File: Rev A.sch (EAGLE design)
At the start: 18 parts

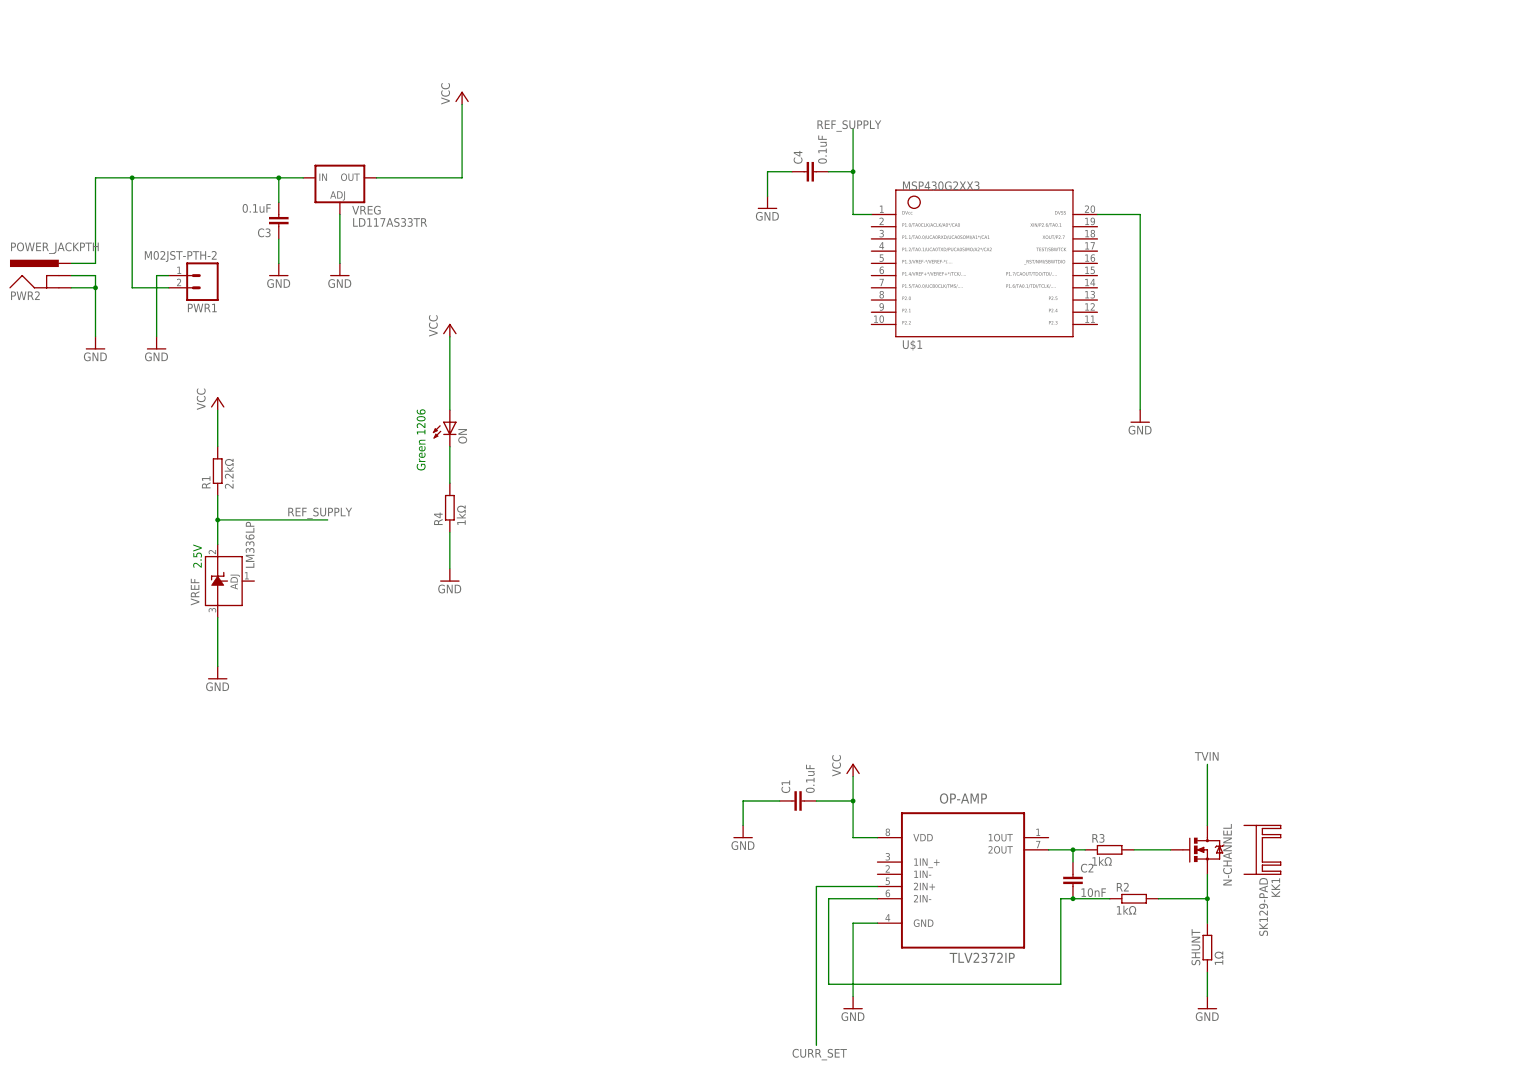
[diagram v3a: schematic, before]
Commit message: Added the PWM filtering circuit
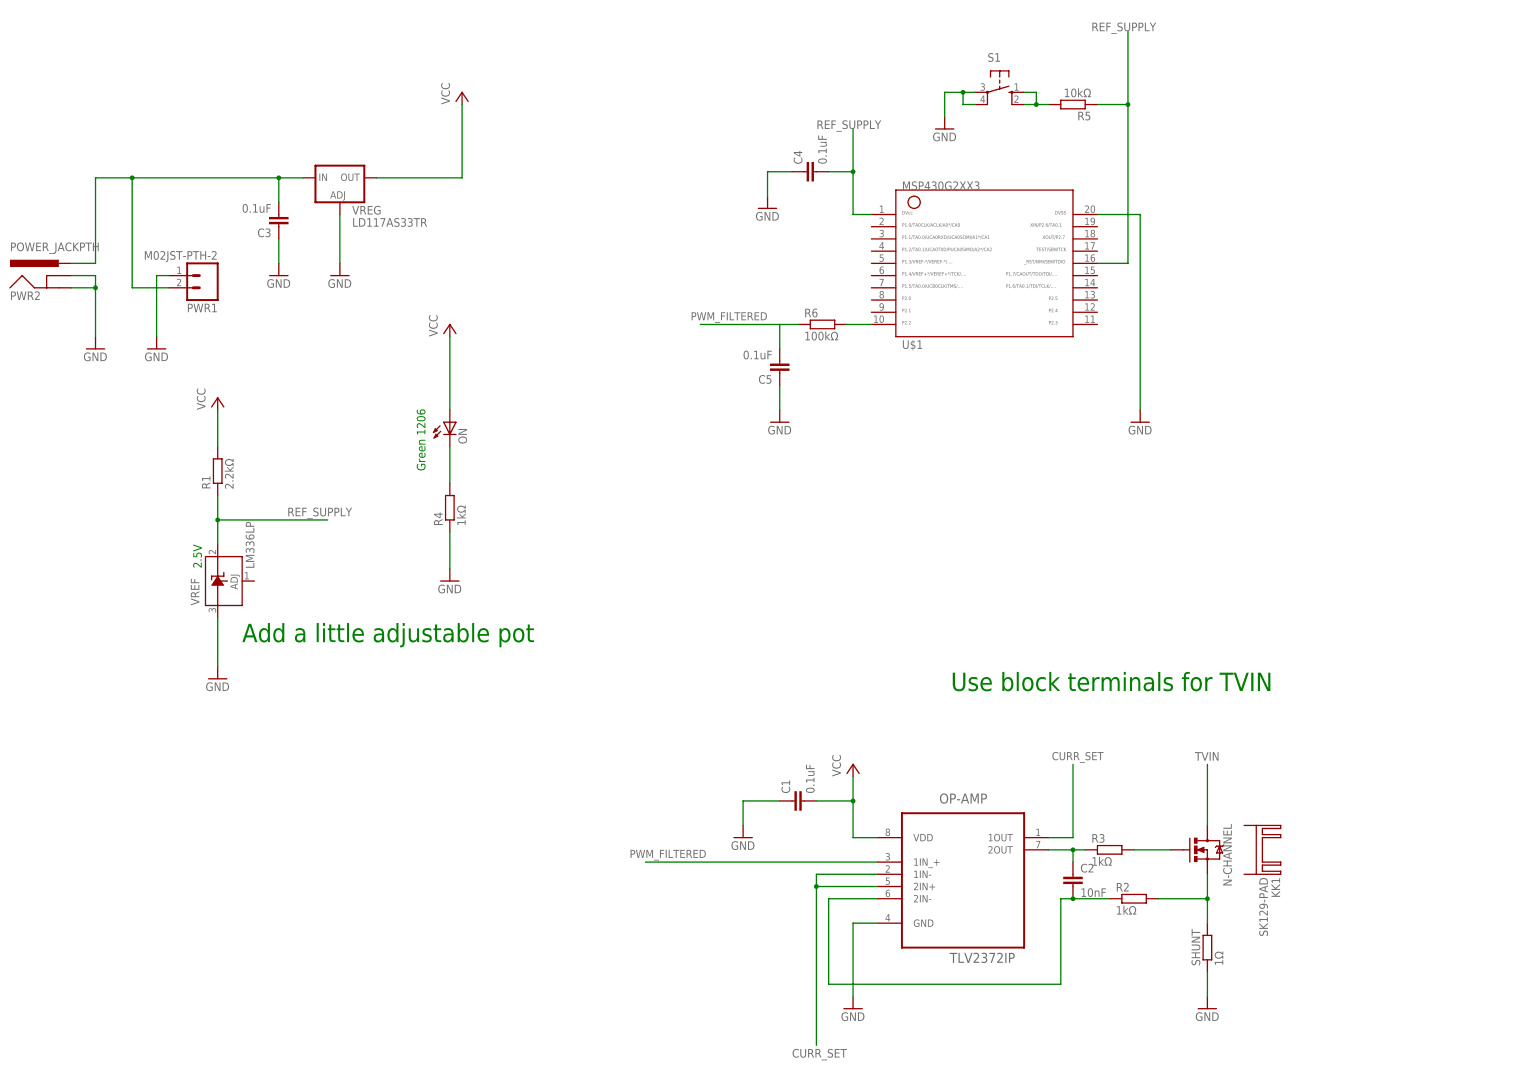
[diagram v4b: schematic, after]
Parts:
- added C5: 0.1uF, rcl:C-EUC0805
- added R5: 10kΩ, resistor:R-EU_R0805
- added R6: 100kΩ, rcl:R-EU_R0805
- added S1: (no value), switch-omron:10-XX
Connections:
- new net N$5: R5.2, S1.S, S1.S1
- new net N$8: R6.2, U$1.10
- new net PWM_FILTERED: C5.2, OP-AMP.1IN_+, R6.1
- net CURR_SET: now also OP-AMP.1IN-, OP-AMP.1OUT
- net GND: now also C5.1, S1.P, S1.P1
- net REF_SUPPLY: now also R5.1, U$1.16
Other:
- note added: "Add a little adjustable pot"
- note added: "Use block terminals for TVIN"
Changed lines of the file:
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@@
 <part name="GND11" library="supply1" deviceset="GND" device=""/>
 <part name="C4" library="rcl" deviceset="C-EU" device="C0805" value="0.1uF"/>
+<part name="S1" library="switch-omron" deviceset="10-XX" device=""/>
+<part name="R5" library="resistor" deviceset="R-EU_" device="R0805" value="10kΩ"/>
+<part name="GND12" library="supply1" deviceset="GND" device=""/>
+<part name="C5" library="rcl" deviceset="C-EU" device="C0805" value="0.1uF"/>
+<part name="R6" library="rcl" deviceset="R-EU_" device="R0805" value="100kΩ"/>
+<part name="GND13" library="supply1" deviceset="GND" device=""/>
 </parts>
 <sheets>
@@
 <text x="-7.62" y="96.52" size="1.778" layer="91" rot="R270">2.5V</text>
 <text x="40.64" y="111.76" size="1.778" layer="91" rot="R90">Green 1206</text>
+<text x="2.54" y="76.2" size="3.81" layer="91">Add a little adjustable pot</text>
+<text x="149.86" y="66.04" size="3.81" layer="91">Use block terminals for TVIN</text>
 </plain>
 <instances>
@@
 <instance part="GND11" gate="1" x="111.76" y="166.37"/>
 <instance part="C4" gate="G$1" x="119.38" y="173.99" rot="R90"/>
+<instance part="S1" gate="1" x="160.02" y="190.5" rot="R270"/>
+<instance part="R5" gate="G$1" x="175.26" y="187.96" rot="R180"/>
+<instance part="GND12" gate="1" x="148.59" y="182.88"/>
+<instance part="C5" gate="G$1" x="114.3" y="132.08" rot="R180"/>
+<instance part="R6" gate="G$1" x="123.19" y="142.24"/>
+<instance part="GND13" gate="1" x="114.3" y="121.92"/>
 </instances>
 <busses>
@@
 <wire x1="116.84" y1="173.99" x2="111.76" y2="173.99" width="0.1524" layer="91"/>
 <wire x1="111.76" y1="173.99" x2="111.76" y2="168.91" width="0.1524" layer="91"/>
+</segment>
+<segment>
+<pinref part="S1" gate="1" pin="P"/>
+<wire x1="154.94" y1="190.5" x2="152.4" y2="190.5" width="0.1524" layer="91"/>
+<wire x1="152.4" y1="190.5" x2="148.59" y2="190.5" width="0.1524" layer="91"/>
+<wire x1="148.59" y1="190.5" x2="148.59" y2="185.42" width="0.1524" layer="91"/>
+<pinref part="GND12" gate="1" pin="GND"/>
+<pinref part="S1" gate="1" pin="P1"/>
+<wire x1="154.94" y1="187.96" x2="152.4" y2="187.96" width="0.1524" layer="91"/>
+<wire x1="152.4" y1="187.96" x2="152.4" y2="190.5" width="0.1524" layer="91"/>
+<junction x="152.4" y="190.5"/>
+</segment>
+<segment>
+<pinref part="C5" gate="G$1" pin="1"/>
+<wire x1="114.3" y1="129.54" x2="114.3" y2="124.46" width="0.1524" layer="91"/>
+<pinref part="GND13" gate="1" pin="GND"/>
 </segment>
 </net>
@@
 <wire x1="121.92" y1="25.4" x2="121.92" y2="-7.62" width="0.1524" layer="91"/>
 <label x="116.84" y="-10.16" size="1.778" layer="95"/>
+<pinref part="OP-AMP" gate="A" pin="1IN-"/>
+<wire x1="134.62" y1="27.94" x2="121.92" y2="27.94" width="0.1524" layer="91"/>
+<wire x1="121.92" y1="27.94" x2="121.92" y2="25.4" width="0.1524" layer="91"/>
+<junction x="121.92" y="25.4"/>
+</segment>
+<segment>
+<pinref part="OP-AMP" gate="A" pin="1OUT"/>
+<wire x1="170.18" y1="35.56" x2="175.26" y2="35.56" width="0.1524" layer="91"/>
+<wire x1="175.26" y1="35.56" x2="175.26" y2="50.8" width="0.1524" layer="91"/>
+<label x="181.61" y="53.34" size="1.6764" layer="95" rot="R180"/>
 </segment>
 </net>
@@
 <wire x1="124.46" y1="173.99" x2="129.54" y2="173.99" width="0.1524" layer="91"/>
 </segment>
+<segment>
+<wire x1="186.69" y1="154.94" x2="186.69" y2="187.96" width="0.1524" layer="91"/>
+<junction x="186.69" y="187.96"/>
+<pinref part="R5" gate="G$1" pin="1"/>
+<wire x1="180.34" y1="187.96" x2="186.69" y2="187.96" width="0.1524" layer="91"/>
+<pinref part="U$1" gate="G$1" pin="16"/>
+<wire x1="186.69" y1="154.94" x2="180.34" y2="154.94" width="0.1524" layer="91"/>
+<wire x1="186.69" y1="187.96" x2="186.69" y2="203.2" width="0.1524" layer="91"/>
+<label x="179.07" y="203.2" size="1.778" layer="95"/>
+</segment>
 </net>
 <net name="N$7" class="0">
@@
 </segment>
 </net>
+<net name="N$5" class="0">
+<segment>
+<pinref part="S1" gate="1" pin="S1"/>
+<pinref part="R5" gate="G$1" pin="2"/>
+<wire x1="165.1" y1="187.96" x2="167.64" y2="187.96" width="0.1524" layer="91"/>
+<pinref part="S1" gate="1" pin="S"/>
+<wire x1="167.64" y1="187.96" x2="170.18" y2="187.96" width="0.1524" layer="91"/>
+<wire x1="165.1" y1="190.5" x2="167.64" y2="190.5" width="0.1524" layer="91"/>
+<wire x1="167.64" y1="190.5" x2="167.64" y2="187.96" width="0.1524" layer="91"/>
+<junction x="167.64" y="187.96"/>
+</segment>
+</net>
+<net name="N$8" class="0">
+<segment>
+<pinref part="U$1" gate="G$1" pin="10"/>
+<pinref part="R6" gate="G$1" pin="2"/>
+<wire x1="133.35" y1="142.24" x2="128.27" y2="142.24" width="0.1524" layer="91"/>
+</segment>
+</net>
+<net name="PWM_FILTERED" class="0">
+<segment>
+<pinref part="R6" gate="G$1" pin="1"/>
+<pinref part="C5" gate="G$1" pin="2"/>
+<wire x1="118.11" y1="142.24" x2="114.3" y2="142.24" width="0.1524" layer="91"/>
+<wire x1="114.3" y1="142.24" x2="114.3" y2="137.16" width="0.1524" layer="91"/>
+<wire x1="114.3" y1="142.24" x2="97.79" y2="142.24" width="0.1524" layer="91"/>
+<label x="111.76" y="144.78" size="1.6764" layer="95" rot="R180"/>
+</segment>
+<segment>
+<pinref part="OP-AMP" gate="A" pin="1IN_+"/>
+<wire x1="134.62" y1="30.48" x2="86.36" y2="30.48" width="0.1524" layer="91"/>
+<label x="99.06" y="33.02" size="1.6764" layer="95" rot="R180"/>
+</segment>
+</net>

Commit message: Started working on the board layout
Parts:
- removed R5: 10kΩ, resistor:R-EU_R0805
- removed S1: (no value), switch-omron:10-XX
- added R7: 10kΩ, resistor:R-EU_R0805
- renumbered U$1 to MCU
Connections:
- removed net N$5: R5.2, S1.S, S1.S1
- new net N$9: MCU.16, R7.2
- net GND: no longer S1.P, S1.P1
- net REF_SUPPLY: now also R7.1; no longer MCU.16, R5.1
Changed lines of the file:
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@@
 <part name="R4" library="rcl" deviceset="R-EU_" device="R0805" value="1kΩ"/>
 <part name="GND9" library="supply1" deviceset="GND" device=""/>
-<part name="U$1" library="TI_MSP430_v16" deviceset="G2XX3---N20" device=""/>
+<part name="MCU" library="TI_MSP430_v16" deviceset="G2XX3---N20" device=""/>
 <part name="GND10" library="supply1" deviceset="GND" device=""/>
 <part name="GND11" library="supply1" deviceset="GND" device=""/>
 <part name="C4" library="rcl" deviceset="C-EU" device="C0805" value="0.1uF"/>
-<part name="S1" library="switch-omron" deviceset="10-XX" device=""/>
-<part name="R5" library="resistor" deviceset="R-EU_" device="R0805" value="10kΩ"/>
-<part name="GND12" library="supply1" deviceset="GND" device=""/>
 <part name="C5" library="rcl" deviceset="C-EU" device="C0805" value="0.1uF"/>
 <part name="R6" library="rcl" deviceset="R-EU_" device="R0805" value="100kΩ"/>
 <part name="GND13" library="supply1" deviceset="GND" device=""/>
+<part name="R7" library="resistor" deviceset="R-EU_" device="R0805" value="10kΩ"/>
 </parts>
 <sheets>
@@
 <instance part="R4" gate="G$1" x="45.72" y="104.14" rot="R90"/>
 <instance part="GND9" gate="1" x="45.72" y="88.9"/>
-<instance part="U$1" gate="G$1" x="157.48" y="157.48"/>
+<instance part="MCU" gate="G$1" x="157.48" y="157.48"/>
 <instance part="GND10" gate="1" x="189.23" y="121.92"/>
 <instance part="GND11" gate="1" x="111.76" y="166.37"/>
 <instance part="C4" gate="G$1" x="119.38" y="173.99" rot="R90"/>
-<instance part="S1" gate="1" x="160.02" y="190.5" rot="R270"/>
-<instance part="R5" gate="G$1" x="175.26" y="187.96" rot="R180"/>
-<instance part="GND12" gate="1" x="148.59" y="182.88"/>
 <instance part="C5" gate="G$1" x="114.3" y="132.08" rot="R180"/>
 <instance part="R6" gate="G$1" x="123.19" y="142.24"/>
 <instance part="GND13" gate="1" x="114.3" y="121.92"/>
+<instance part="R7" gate="G$1" x="186.69" y="182.88" rot="R270"/>
 </instances>
 <busses>
@@
 </segment>
 <segment>
-<pinref part="U$1" gate="G$1" pin="20"/>
+<pinref part="MCU" gate="G$1" pin="20"/>
 <wire x1="180.34" y1="165.1" x2="189.23" y2="165.1" width="0.1524" layer="91"/>
 <wire x1="189.23" y1="165.1" x2="189.23" y2="124.46" width="0.1524" layer="91"/>
@@
 <wire x1="116.84" y1="173.99" x2="111.76" y2="173.99" width="0.1524" layer="91"/>
 <wire x1="111.76" y1="173.99" x2="111.76" y2="168.91" width="0.1524" layer="91"/>
-</segment>
-<segment>
-<pinref part="S1" gate="1" pin="P"/>
-<wire x1="154.94" y1="190.5" x2="152.4" y2="190.5" width="0.1524" layer="91"/>
-<wire x1="152.4" y1="190.5" x2="148.59" y2="190.5" width="0.1524" layer="91"/>
-<wire x1="148.59" y1="190.5" x2="148.59" y2="185.42" width="0.1524" layer="91"/>
-<pinref part="GND12" gate="1" pin="GND"/>
-<pinref part="S1" gate="1" pin="P1"/>
-<wire x1="154.94" y1="187.96" x2="152.4" y2="187.96" width="0.1524" layer="91"/>
-<wire x1="152.4" y1="187.96" x2="152.4" y2="190.5" width="0.1524" layer="91"/>
-<junction x="152.4" y="190.5"/>
 </segment>
 <segment>
@@
 </segment>
 <segment>
-<pinref part="U$1" gate="G$1" pin="1"/>
+<pinref part="MCU" gate="G$1" pin="1"/>
 <wire x1="133.35" y1="165.1" x2="129.54" y2="165.1" width="0.1524" layer="91"/>
 <wire x1="129.54" y1="165.1" x2="129.54" y2="173.99" width="0.1524" layer="91"/>
@@
 </segment>
 <segment>
-<wire x1="186.69" y1="154.94" x2="186.69" y2="187.96" width="0.1524" layer="91"/>
-<junction x="186.69" y="187.96"/>
-<pinref part="R5" gate="G$1" pin="1"/>
-<wire x1="180.34" y1="187.96" x2="186.69" y2="187.96" width="0.1524" layer="91"/>
-<pinref part="U$1" gate="G$1" pin="16"/>
-<wire x1="186.69" y1="154.94" x2="180.34" y2="154.94" width="0.1524" layer="91"/>
-<wire x1="186.69" y1="187.96" x2="186.69" y2="203.2" width="0.1524" layer="91"/>
-<label x="179.07" y="203.2" size="1.778" layer="95"/>
+<pinref part="R7" gate="G$1" pin="1"/>
+<wire x1="186.69" y1="187.96" x2="186.69" y2="201.93" width="0.1524" layer="91"/>
+<label x="193.04" y="204.47" size="1.6764" layer="95" rot="R180"/>
 </segment>
 </net>
@@
 </segment>
 </net>
-<net name="N$5" class="0">
-<segment>
-<pinref part="S1" gate="1" pin="S1"/>
-<pinref part="R5" gate="G$1" pin="2"/>
-<wire x1="165.1" y1="187.96" x2="167.64" y2="187.96" width="0.1524" layer="91"/>
-<pinref part="S1" gate="1" pin="S"/>
-<wire x1="167.64" y1="187.96" x2="170.18" y2="187.96" width="0.1524" layer="91"/>
-<wire x1="165.1" y1="190.5" x2="167.64" y2="190.5" width="0.1524" layer="91"/>
-<wire x1="167.64" y1="190.5" x2="167.64" y2="187.96" width="0.1524" layer="91"/>
-<junction x="167.64" y="187.96"/>
-</segment>
-</net>
 <net name="N$8" class="0">
 <segment>
-<pinref part="U$1" gate="G$1" pin="10"/>
+<pinref part="MCU" gate="G$1" pin="10"/>
 <pinref part="R6" gate="G$1" pin="2"/>
 <wire x1="133.35" y1="142.24" x2="128.27" y2="142.24" width="0.1524" layer="91"/>
@@
 </segment>
 </net>
+<net name="N$9" class="0">
+<segment>
+<pinref part="MCU" gate="G$1" pin="16"/>
+<pinref part="R7" gate="G$1" pin="2"/>
+<wire x1="180.34" y1="154.94" x2="186.69" y2="154.94" width="0.1524" layer="91"/>
+<wire x1="186.69" y1="154.94" x2="186.69" y2="177.8" width="0.1524" layer="91"/>
+</segment>
+</net>

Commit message: Modified some stuff in the schematic
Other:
- note added: "Check if the opamp VCC being higher than the MCU VCC will amplify the thing."
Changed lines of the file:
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@@
 <setting verticaltext="up"/>
 </settings>
-<grid distance="0.05" unitdist="inch" unit="inch" style="lines" multiple="1" display="no" altdistance="0.01" altunitdist="inch" altunit="inch"/>
+<grid distance="0.1" unitdist="inch" unit="inch" style="lines" multiple="1" display="no" altdistance="0.01" altunitdist="inch" altunit="inch"/>
 <layers>
 <layer number="1" name="Top" color="4" fill="1" visible="no" active="no"/>
@@
 <text x="2.54" y="76.2" size="3.81" layer="91">Add a little adjustable pot</text>
 <text x="149.86" y="66.04" size="3.81" layer="91">Use block terminals for TVIN</text>
+<text x="20.32" y="48.26" size="3.81" layer="91">Check if the opamp VCC
+being higher than the MCU
+VCC will amplify the thing.</text>
 </plain>
 <instances>
@@
 </schematic>
 </drawing>
+<compatibility>
+<note version="6.3" minversion="6.2.2" severity="warning">
+Since Version 6.2.2 text objects can contain more than one line,
+which will not be processed correctly with this version.
+</note>
+</compatibility>
 </eagle>
